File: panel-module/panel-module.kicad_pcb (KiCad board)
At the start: 2 copper layers, 40.6 x 30.4 mm, 20 parts, among them J1 East, J2 West, J3 Debug, J4 Display, SW1 Setup, SW2 Reset

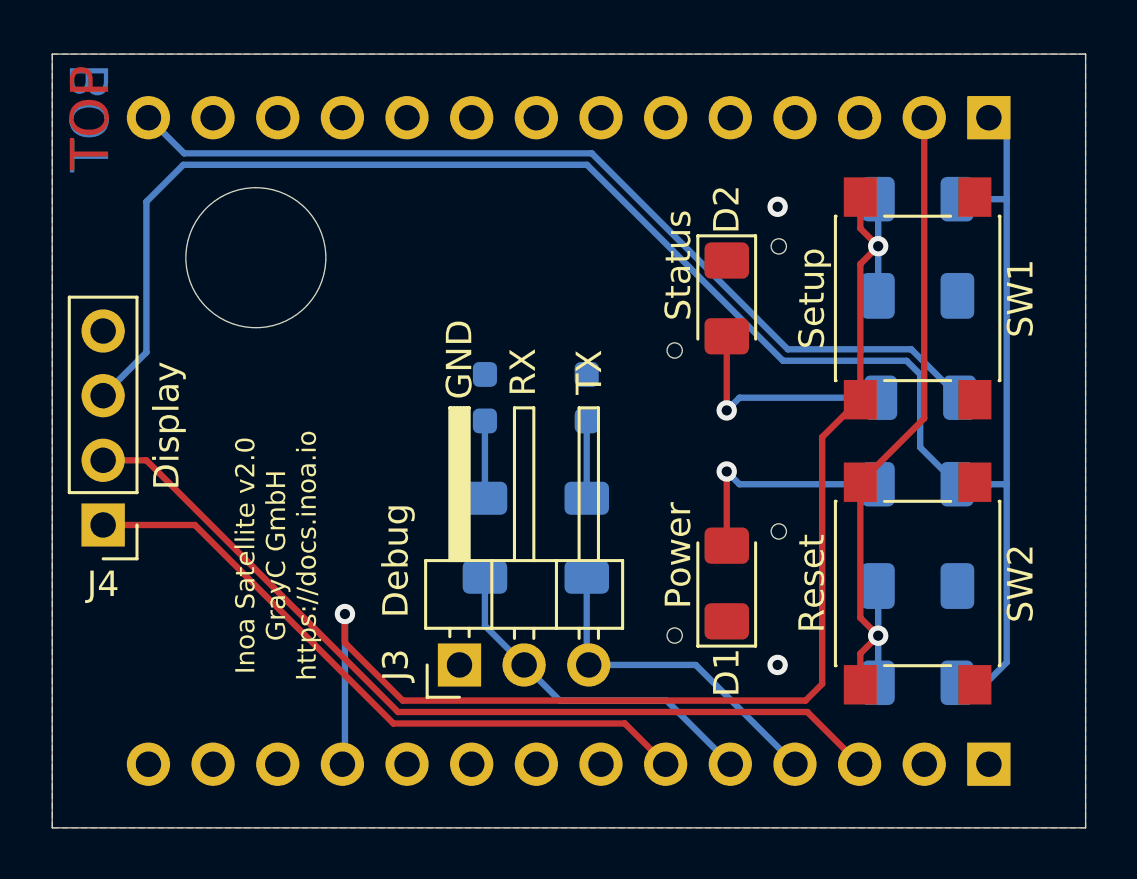
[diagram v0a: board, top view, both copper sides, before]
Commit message: Better Silk placings for Panel Module
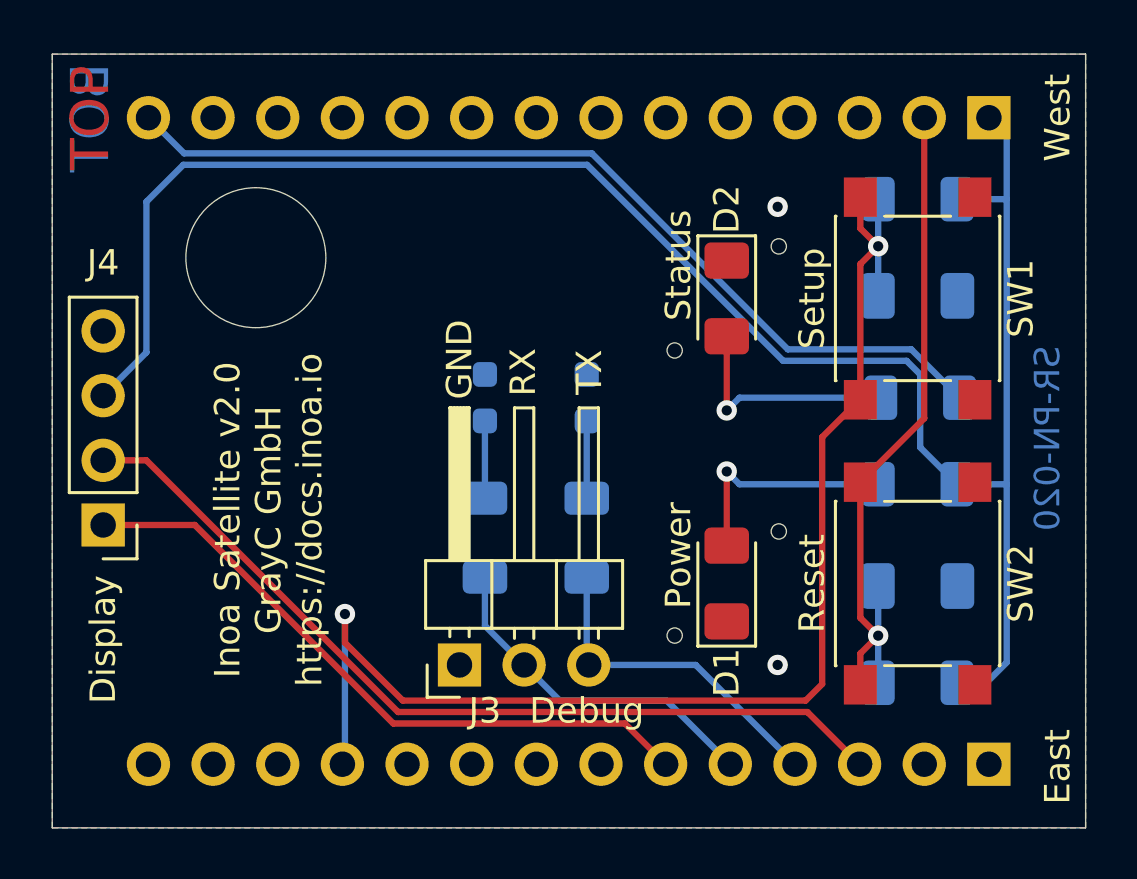
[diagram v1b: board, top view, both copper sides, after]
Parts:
- moved G1 21.2 mm to (138.5, 88.0)
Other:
- board text added: "East"
- board text added: "SR-PN-020"
- board text added: "West"

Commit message: Added OpenHardware Logo to PCBs
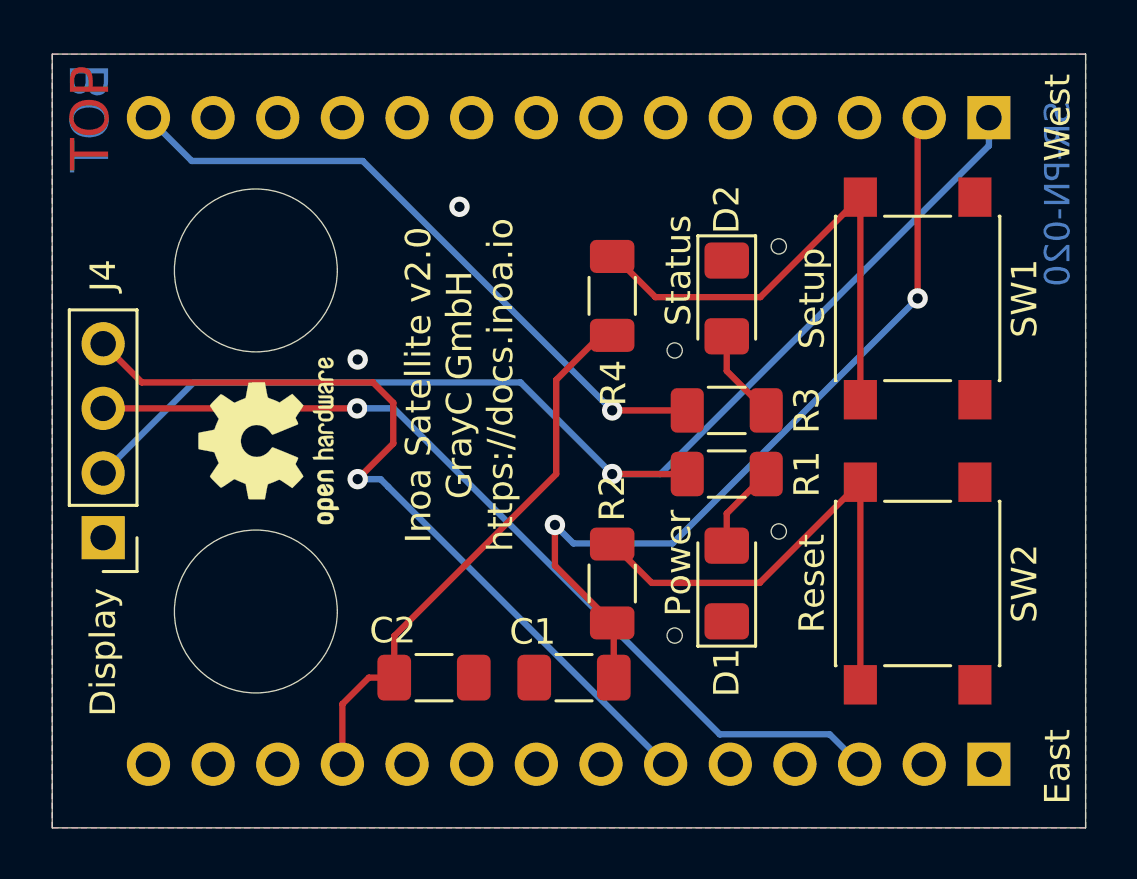
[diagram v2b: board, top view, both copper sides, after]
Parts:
- removed D3, D4: ESD3.3, Resistor_SMD:R_0603_1608Metric_Pad0.98x0.95mm_HandSolder
- removed J3: Debug, Connector_PinHeader_2.54mm:PinHeader_1x03_P2.54mm_Horizontal
- removed R5: 220R, Resistor_SMD:R_1206_3216Metric_Pad1.30x1.75mm_HandSolder
- removed R6: 10k, Resistor_SMD:R_1206_3216Metric_Pad1.30x1.75mm_HandSolder
- added G2: Logo_Open_Hardware_Small, Symbol:OSHW-Logo2_7.3x6mm_SilkScreen, F.Cu at (128.5, 95.2)
- added H2: LoRa, MountingHole:MountingHole_6.4mm_M6, F.Cu at (128.0, 101.9)
- C1, R1, R3: moved to F.Cu
- C2: value 2u2 -> 0u1; moved to F.Cu
- G1: moved to B.Cu
- H1: value Antenna -> Wifi; footprint footprints:MountingHole_5.5mm_No_Bound -> MountingHole:MountingHole_6.4mm_M6
- R2: value 10k -> 1k; moved to F.Cu
- R4: value 220R -> 1k; moved to F.Cu
- moved C2 24.2 mm to (135.0, 104.5)
- moved G1 23.0 mm to (156.0, 103.0), turned to 270 degrees
- moved R2 19.3 mm to (142.0, 100.8), turned to 90 degrees
- moved C1 14.0 mm to (140.5, 104.5), turned to 180 degrees
- moved R4 10.7 mm to (142.0, 89.5)
- moved R3 7.62 mm to (146.5, 94.0), turned to 0 degrees
- moved R1 7.51 mm to (146.5, 96.5), turned to 0 degrees
- moved H1 0.50 mm to (128.0, 88.5)
- moved J4 0.50 mm to (122.0, 99.0)
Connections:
- J4 pad 1: I2C_SDA -> GND
- J4 pad 2: I2C_SCL -> +3V3
- J4 pad 3: +3V3 -> I2C_SCL
- J4 pad 4: GND -> I2C_SDA
- R2 pad 1: +3V3 -> Panel_Reset
- R2 pad 2: Panel_Setup -> Net-(R2-Pad2)
- R4 pad 1: U0RXD -> Panel_Setup
- R4 pad 2: Net-(D3-Pad1) -> Net-(R4-Pad2)
- SW1 pad 2: Panel_Setup -> Net-(R4-Pad2)
- SW2 pad 2: Panel_Reset -> Net-(R2-Pad2)
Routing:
- net Panel_Setup: track 51.2 -> 22.2 mm, vias 2 -> 0
- net +3V3: track 75.5 -> 47.2 mm, vias 0 -> 1
- net Net-(R2-Pad2): track 0.00 -> 20.8 mm
- net Net-(R4-Pad2): track 0.00 -> 20.0 mm
- net U0RXD: track 13.8 -> 0.00 mm
- net U0TXD: track 13.2 -> 0.00 mm
- net Panel_Status: track 36.4 -> 25.9 mm, vias 0 -> 1
- net I2C_SDA: track 26.0 -> 32.7 mm, vias 0 -> 1
- net Net-(D2-Pad2): track 9.17 -> 3.55 mm, vias 1 -> 0
- net Net-(D1-Pad2): track 9.07 -> 3.45 mm, vias 1 -> 0
- net Panel_Reset: track 27.7 -> 32.9 mm, vias 1 -> 2
- net Net-(D4-Pad1): track 3.04 -> 0.00 mm
- net Net-(D3-Pad1): track 3.04 -> 0.00 mm
- net I2C_SCL: track 34.7 -> 35.5 mm, vias 0 -> 1
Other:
- board text removed: "GND"
- board text removed: "RX"
- board text removed: "TX"

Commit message: Feature/kicad 6 migration (#1)
* Adjust CI/CD jobs to use KiCad 6

* Migrate panel module project

* Unify KiBot config

* Migrate Ethernet, SoC, Metering Modules to KiCad6

* Change build order to find out more about strange behavior

* Trigger build also on workflow changes

* Try to increase log level to track error

* Switch to KiCad 6 schematic files

* Fix / Ignore Errors in panel module

* Disable cost calculation for now

* Fixing more ERC errors

* Remove outdated files and settings

* Trim further warnings and errors

* Update documentation
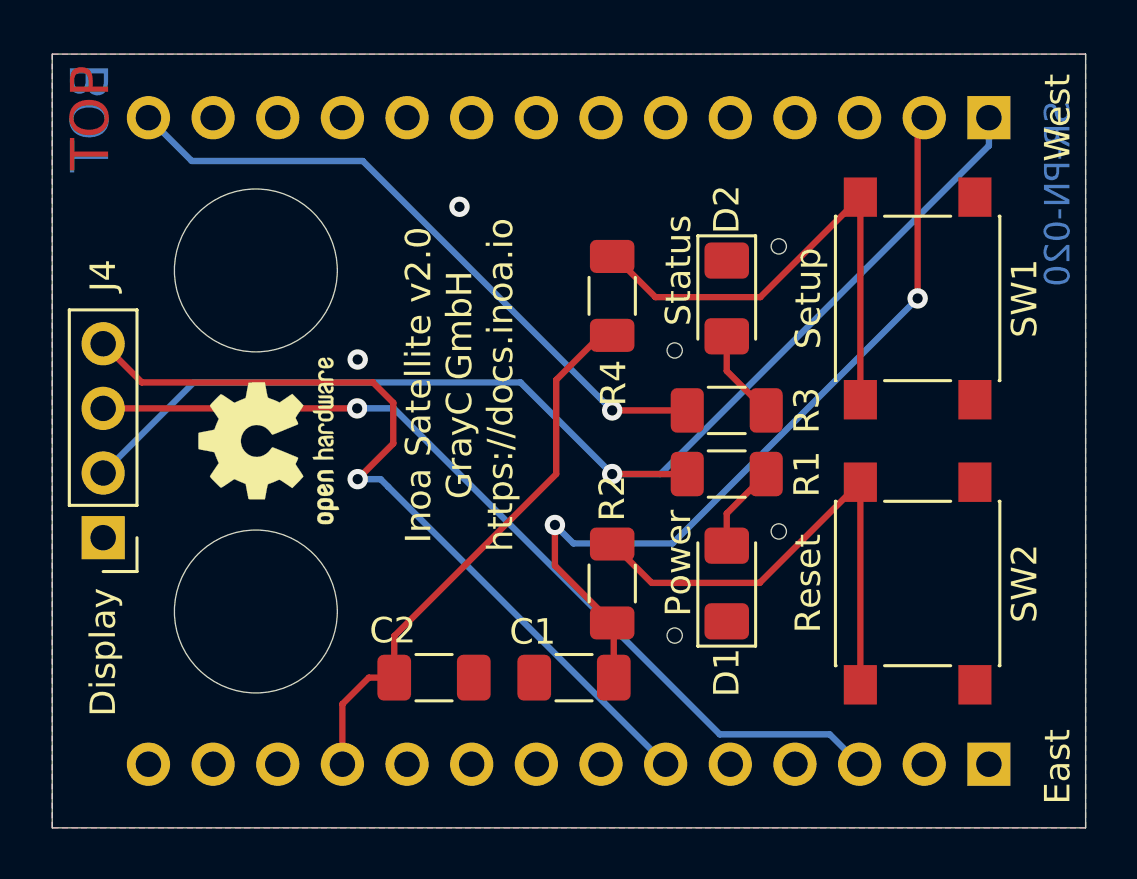
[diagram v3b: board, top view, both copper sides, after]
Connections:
- J1 pad 10: Net-(J1-Pad10) -> unconnected-(J1-Pad10)
- J1 pad 12: Net-(J1-Pad12) -> unconnected-(J1-Pad12)
- J1 pad 13: Net-(J1-Pad13) -> unconnected-(J1-Pad13)
- J1 pad 14: Net-(J1-Pad14) -> unconnected-(J1-Pad14)
- J1 pad 2: Net-(J1-Pad2) -> unconnected-(J1-Pad2)
- J1 pad 4: U0TXD -> unconnected-(J1-Pad4)
- J1 pad 5: U0RXD -> unconnected-(J1-Pad5)
- J1 pad 7: Net-(J1-Pad7) -> unconnected-(J1-Pad7)
- J1 pad 8: Net-(J1-Pad8) -> unconnected-(J1-Pad8)
- J1 pad 9: Net-(J1-Pad9) -> unconnected-(J1-Pad9)
- J2 pad 10: Net-(J2-Pad10) -> unconnected-(J2-Pad10)
- J2 pad 11: Net-(J2-Pad11) -> unconnected-(J2-Pad11)
- J2 pad 12: Net-(J2-Pad12) -> unconnected-(J2-Pad12)
- J2 pad 13: Net-(J2-Pad13) -> unconnected-(J2-Pad13)
- J2 pad 3: Net-(J2-Pad3) -> unconnected-(J2-Pad3)
- J2 pad 4: Net-(J2-Pad4) -> unconnected-(J2-Pad4)
- J2 pad 5: Net-(J2-Pad5) -> unconnected-(J2-Pad5)
- J2 pad 6: Net-(J2-Pad6) -> unconnected-(J2-Pad6)
- J2 pad 7: Net-(J2-Pad7) -> unconnected-(J2-Pad7)
- J2 pad 8: Net-(J2-Pad8) -> unconnected-(J2-Pad8)
- J2 pad 9: Net-(J2-Pad9) -> unconnected-(J2-Pad9)
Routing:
- net Net-(R2-Pad2): track 20.8 -> 20.0 mm
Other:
- net class Default removed
